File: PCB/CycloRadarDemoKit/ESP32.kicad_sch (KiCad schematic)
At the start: 1 part, among them U101 ESP32-WROVER-E

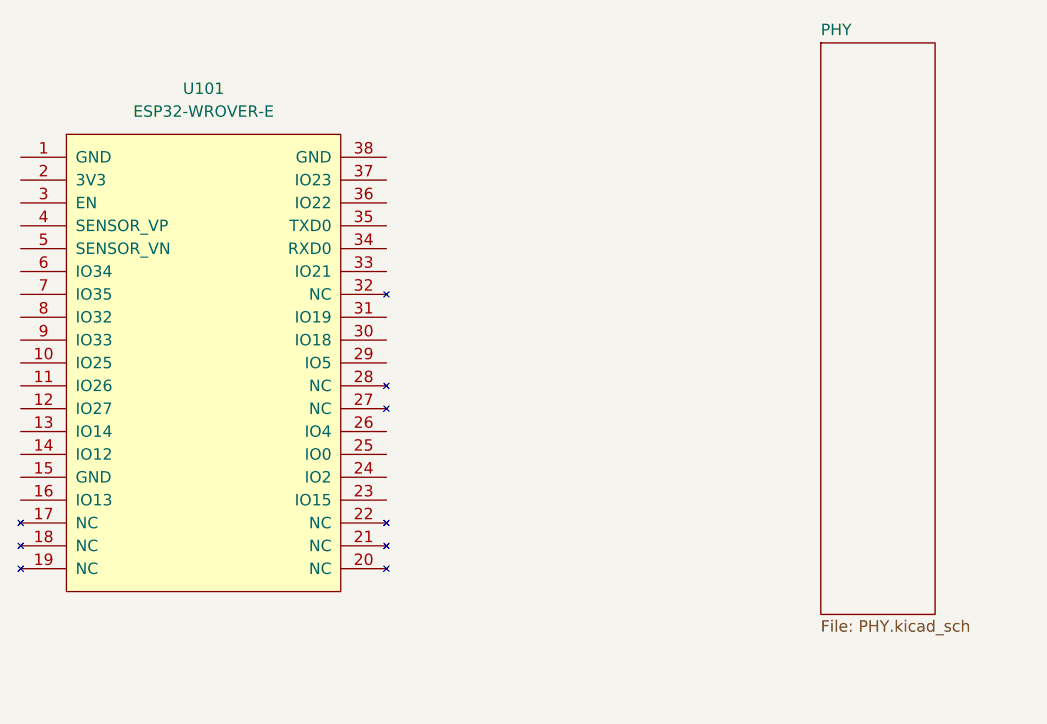
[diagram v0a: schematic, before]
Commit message: PM ICs choosed
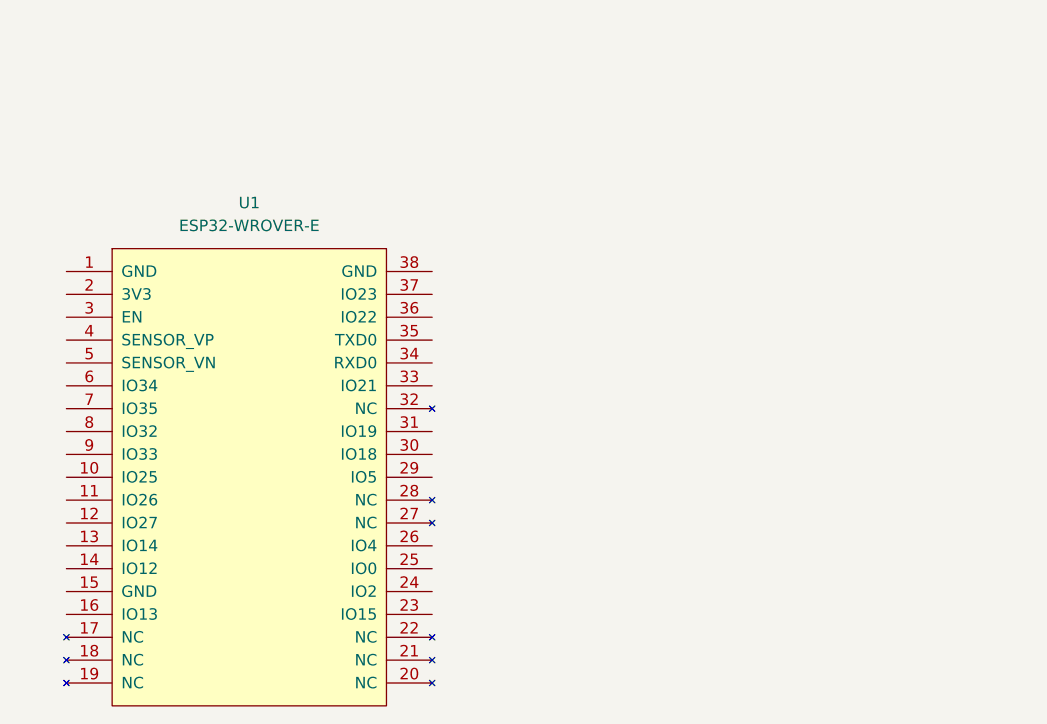
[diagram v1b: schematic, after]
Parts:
- removed U101: ESP32-WROVER-E, EspressIf:ESP32-WROVER-IE, symbol EspressIf:ESP32-WROVER-E
- added U1: ESP32-WROVER-E, symbol EspressIf:ESP32-WROVER-E
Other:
- removed sheet PHY
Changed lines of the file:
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@@
 (kicad_sch (version 20230121) (generator eeschema)
   (paper "A4")
-  (symbol (lib_id "EspressIf:ESP32-WROVER-E") (at 147.32 83.82 0) (unit 1)
+  (symbol (lib_id "EspressIf:ESP32-WROVER-E") (at 152.4 96.52 0) (unit 1)
     (in_bom yes) (on_board yes) (dnp no) (fields_autoplaced)
-    (property "Reference" "U101" (at 147.32 53.34 0)
+    (property "Reference" "U1" (at 152.4 66.04 0)
       (effects (font (size 1.27 1.27)))
     )
-    (property "Value" "ESP32-WROVER-E" (at 147.32 55.88 0)
+    (property "Value" "ESP32-WROVER-E" (at 152.4 68.58 0)
       (effects (font (size 1.27 1.27)))
     )
-    (property "Footprint" "EspressIf:ESP32-WROVER-IE" (at 147.32 74.93 0)
+    (property "Footprint" "" (at 152.4 87.63 0)
       (effects (font (size 1.27 1.27)) hide)
     )
-    (property "Datasheet" "" (at 147.32 74.93 0)
+    (property "Datasheet" "" (at 152.4 87.63 0)
       (effects (font (size 1.27 1.27)) hide)
     )
@@
       (project "CycloRadarDemoKit"
         (path "/c2cd7ca4-4652-4b3d-a3a8-1cfa66cb11e9"
-          (reference "U101") (unit 1)
+          (reference "U1") (unit 1)
         )
         (path "/c2cd7ca4-4652-4b3d-a3a8-1cfa66cb11e9/8ae18a6c-482d-4e1c-94d1-12de0ef4fa68"
@@
     )
   )
-  (sheet (at 215.9 48.26) (size 12.7 63.5) (fields_autoplaced)
-    (stroke (width 0.1524) (type solid))
-    (fill (color 0 0 0 0.0000))
-    (property "Sheetname" "PHY" (at 215.9 47.5484 0)
-      (effects (font (size 1.27 1.27)) (justify left bottom))
-    )
-    (property "Sheetfile" "PHY.kicad_sch" (at 215.9 112.3446 0)
-      (effects (font (size 1.27 1.27)) (justify left top))
-    )
-    (instances
-      (project "CycloRadarDemoKit"
-        (path "/c2cd7ca4-4652-4b3d-a3a8-1cfa66cb11e9" (page "2"))
-      )
-    )
-  )
-  (sheet_instances
-    (path "/" (page "1"))
-  )
 )
